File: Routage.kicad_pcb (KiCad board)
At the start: 2 copper layers, 110 x 100 mm, 52 parts, among them J2 Conn_01x02, J3 Conn_01x03, Q1 2N2907, Q10 TIP32, Q11 BD138, Q12 TIP31, Q13 2N2222, Q2 2N2907, Q3 2N2907, Q4 2N2222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

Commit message: routage v2
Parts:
- moved Q10 67.4 mm to (125.7, 88.9)
- moved Q12 67.3 mm to (59.7, 87.6)
- moved R11 66.0 mm to (132.1, 67.3), turned to 180 degrees
- moved R12 28.1 mm to (83.8, 68.6), turned to 180 degrees
- moved R6 11.4 mm to (108.0, 142.2), turned to 180 degrees
- moved Dz1 10.2 mm to (45.7, 104.1), turned to 270 degrees
- moved R1 10.2 mm to (57.1, 133.3), turned to 270 degrees
- moved R4 10.2 mm to (73.7, 111.8), turned to 270 degrees
- moved R9 10.2 mm to (77.5, 111.8), turned to 270 degrees
- moved R16 8.89 mm to (83.8, 78.7), turned to 270 degrees
- moved R13 2.54 mm to (82.5, 64.8)
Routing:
- net GND: track 0.00 -> 444.5 mm
- net -12V: track 0.00 -> 341.8 mm
- net +12V: track 0.00 -> 321.7 mm
- net /Sorti_Push_Pull: track 0.00 -> 155.6 mm
- net /Q5_Q8_Q4_C2: track 0.00 -> 146.5 mm
- net Net-(Q2-Pad2): track 0.00 -> 112.3 mm
- net /RV1_Q8_Q6: track 0.00 -> 75.7 mm
- net /Sortie_EtageDiff: track 0.00 -> 59.2 mm
- net /Q7_Q6: track 0.00 -> 45.1 mm
- net /Q10_Q9_R11: track 0.00 -> 37.2 mm
- net /C1_R1_Q1: track 0.00 -> 33.4 mm
- net Net-(D1-Pad2): track 0.00 -> 29.6 mm
- net /R16_C3_D2: track 0.00 -> 29.1 mm
- net /Q9_Q10: track 0.00 -> 27.1 mm
- net /Q11_Q12_R12: track 0.00 -> 26.4 mm
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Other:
- net class alim diff added: clearance 0.3, trace_width 1, via_dia 1.9, via_drill 0.6
- net class alim push pull added: clearance 0.3, trace_width 2.1, via_dia 1.9, via_drill 0.6
- net class etage diff ec added: clearance 0.3, trace_width 0.6, via_dia 1.9, via_drill 0.6
- rule trace_min: 0.2 -> 0.4
- rule via_min_size: 0.4 -> 0.6

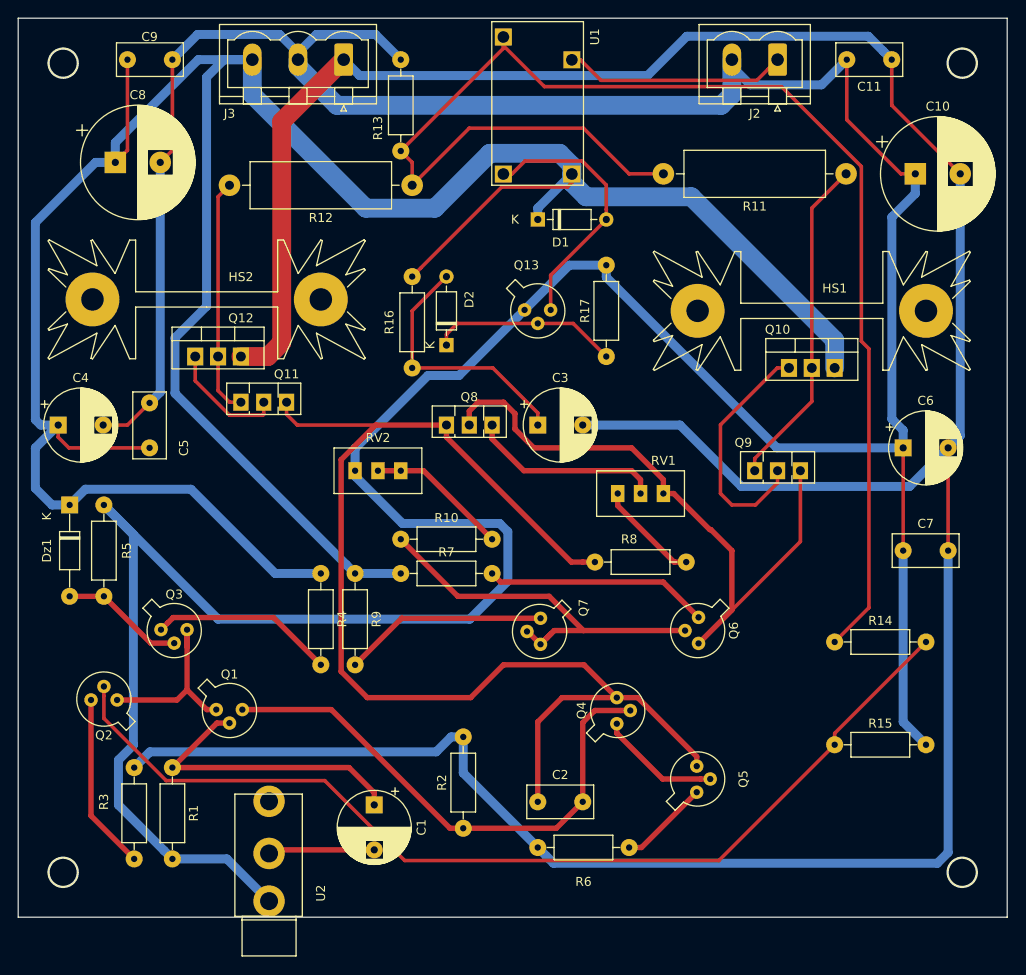
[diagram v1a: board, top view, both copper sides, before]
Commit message: routage modifie
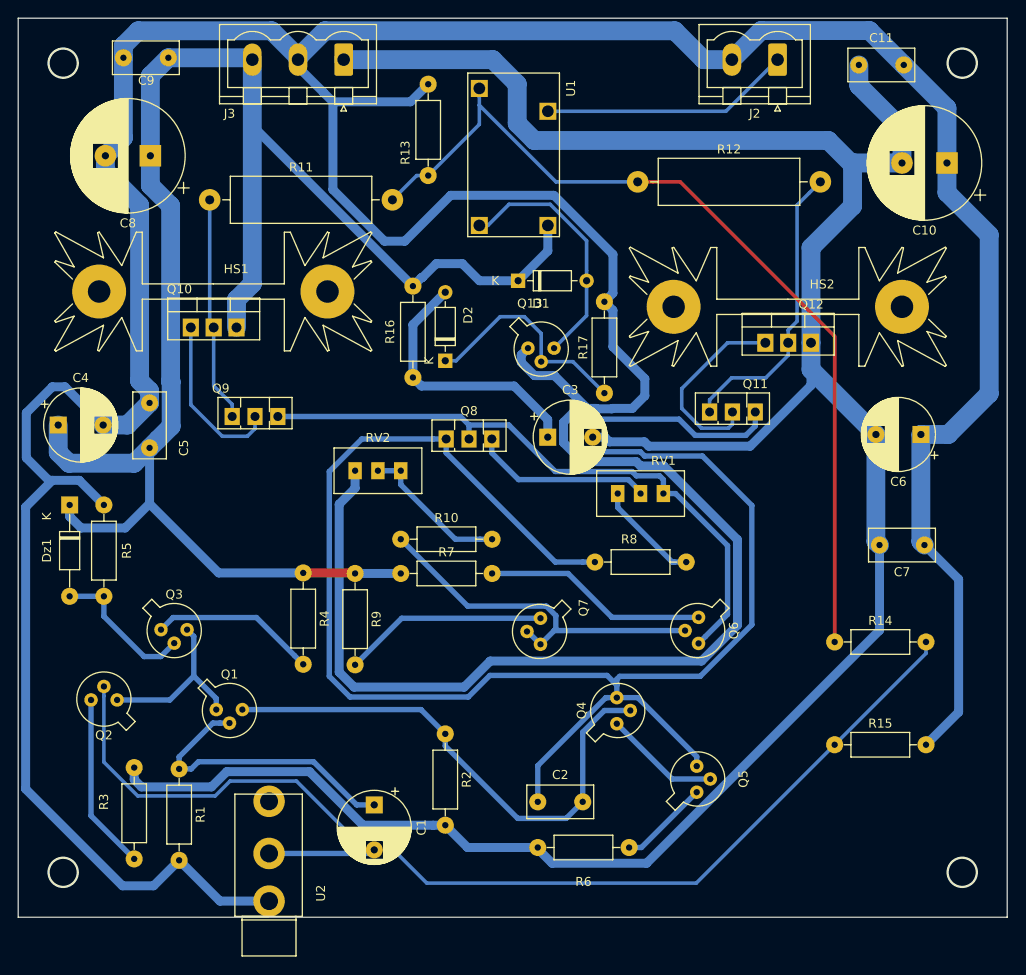
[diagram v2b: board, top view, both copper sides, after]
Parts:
- moved R11 70.8 mm to (61.3, 70.2), turned to 0 degrees
- moved Q10 66.7 mm to (59.2, 84.4)
- moved HS1 66.6 mm to (61.7, 80.4)
- moved HS2 64.6 mm to (125.6, 82.1)
- moved Q12 63.4 mm to (123.1, 86.1)
- moved Q9 58.4 mm to (63.8, 94.3)
- moved Q11 52.1 mm to (116.9, 93.8)
- moved R12 25.1 mm to (108.9, 68.2), turned to 0 degrees
- moved R2 10.7 mm to (87.5, 129.6), turned to 270 degrees
- moved D1 7.15 mm to (95.6, 79.2)
- moved U1 6.31 mm to (100.2, 74.3)
- moved C9 5.45 mm to (51.7, 54.4), turned to 0 degrees
- moved Q13 4.27 mm to (96.9, 86.8)
- moved R13 4.09 mm to (85.6, 67.5)
- moved R17 4.08 mm to (105.2, 91.7)
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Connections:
- net Net-(D1-Pad2) renamed /Relay_Q13
- net Net-(Q2-Pad2) renamed /Q2_R14_R15
- net Net-(Q2-Pad3) renamed /Q2_R3
- net Net-(Q8-Pad3) renamed /Q8_RV2
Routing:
- net +12V: track 321.7 -> 203.7 mm
- net GND: track 444.5 -> 540.9 mm
- net -12V: track 341.8 -> 268.9 mm
- net /Q5_Q8_Q4_C2: track 146.5 -> 203.1 mm
- net /Sorti_Push_Pull: track 155.6 -> 101.3 mm
- net /Q10_Q9_R11: track 37.2 -> 25.1 mm
- net /Q11_Q12: track 13.3 -> 21.7 mm
- net /Q9_Q10: track 27.1 -> 18.9 mm
- net /Q11_Q12_R12: track 26.4 -> 32.9 mm
- net /Q2_R14_R15: track 112.3 -> 118.6 mm
- net /RV1_Q8_Q6: track 75.7 -> 70.6 mm
- net /Q13_R17: track 21.0 -> 25.1 mm
- net /Q7_Q6: track 45.1 -> 41.3 mm
- net /Relay_J2: track 24.8 -> 27.9 mm
- net /Dz1_R5_Q3: track 13.8 -> 16.3 mm
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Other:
- net class Alim+12 added: clearance 0.3, trace_width 0.4, via_dia 1.9, via_drill 0.6
- net class Alim-12 added: clearance 0.3, trace_width 0.4, via_dia 1.9, via_drill 0.6
- net class Etage Diff added: clearance 0.3, trace_width 0.6, via_dia 1.9, via_drill 0.6
- net class Etage EC added: clearance 0.3, trace_width 0.6, via_dia 1.9, via_drill 0.6
- net class Etage Push Pull added: clearance 0.3, trace_width 0.4, via_dia 1.9, via_drill 0.6
- net class Etage Relay added: clearance 0.3, trace_width 0.4, via_dia 1.9, via_drill 0.6
- net class GND added: clearance 0.3, trace_width 0.4, via_dia 1.9, via_drill 0.6
- net class alim diff removed
- net class alim push pull removed
- net class etage diff ec removed

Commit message: Routage modifie 2
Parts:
- moved C4 5.85 mm to (50.0, 97.1), turned to 180 degrees
- moved RV1 4.43 mm to (111.8, 107.3)
- moved Q7 3.24 mm to (94.8, 117.5), turned to 0 degrees
- moved R8 2.01 mm to (105.2, 112.2)
- moved Q3 1.72 mm to (57.3, 116.9), turned to 270 degrees
- moved Q13 0.70 mm to (96.9, 87.5), turned to 90 degrees
- moved HS1 0.20 mm to (61.7, 80.2)
- moved HS2 0.20 mm to (125.6, 81.9)
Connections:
- J2 pad 1: /Relay_J2 -> GND
- J2 pad 2: GND -> /Relay_J2
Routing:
- net +12V: track 203.7 -> 235.0 mm
- net -12V: track 268.9 -> 280.2 mm
- net GND: track 540.9 -> 536.1 mm, vias 0 -> 10
- net /Dz1_R5_Q3: track 16.3 -> 11.8 mm
- net /Q13_R17: track 25.1 -> 20.8 mm
- net /Q7_R9: track 22.8 -> 19.0 mm
- net /Relay_J2: track 27.9 -> 25.1 mm
- net /Q11_Q12: track 21.7 -> 18.9 mm
- net /Q8_RV2: track 20.1 -> 22.7 mm
- net /C1_R1_Q1: track 32.5 -> 34.8 mm
- net /Q3_R4: track 18.5 -> 16.4 mm
- net /Sorti_Push_Pull: track 101.3 -> 103.4 mm, vias 0 -> 2
- net /Relay_Q13: track 28.0 -> 30.0 mm
- net /Q5_Q8_Q4_C2: track 203.1 -> 204.7 mm
- net /RV1_Q8_Q6: track 70.6 -> 69.1 mm
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- added copper zone on B.Cu, net (none)
- added copper zone on B.Cu, net GND
- added copper zone on F.Cu, net GND
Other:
- board text added: "Ampli Audio Maxime Ramiara Yiannis Manzo Lenny Laffargue 3 IMACS E"

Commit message: version finale
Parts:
- moved R14 46.4 mm to (125.2, 73.3)
- moved R7 10.1 mm to (72.5, 111.8)
- moved R9 8.37 mm to (72.5, 118.5), turned to 0 degrees
- moved R4 4.50 mm to (67.2, 111.8)
- moved R12 3.41 mm to (106.3, 66.0)
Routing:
- net /Q2_R14_R15: track 119.5 -> 173.1 mm
- net /Sorti_Push_Pull: track 103.4 -> 62.6 mm, vias 2 -> 0
- net /Q6_R7: track 25.0 -> 35.0 mm
- net /Q7_R9: track 19.0 -> 12.4 mm
- net /Q3_R4: track 16.4 -> 12.0 mm
- net /Q7_Q6: track 40.7 -> 44.8 mm
- net +12V: track 235.0 -> 231.8 mm
- net /Q11_Q12_R12: track 32.9 -> 35.9 mm
- net /RV1_Q8_Q6: track 69.1 -> 70.3 mm
